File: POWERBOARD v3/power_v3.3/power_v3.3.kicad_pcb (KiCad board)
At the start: 4 copper layers, 60 x 34.1 mm, 63 parts, among them IC1 MAX25301AATB_V+T, IC2 MCP6541T-I_OT, IC3 AP2281-1FMG-7, J1 43650-0300, J2 UJ20-C-H-G-SMT-1-P16-TR, J3 2053380002, U1 USBLC6-2, U2 BQ25886RGE, U3 TPS62160DSG

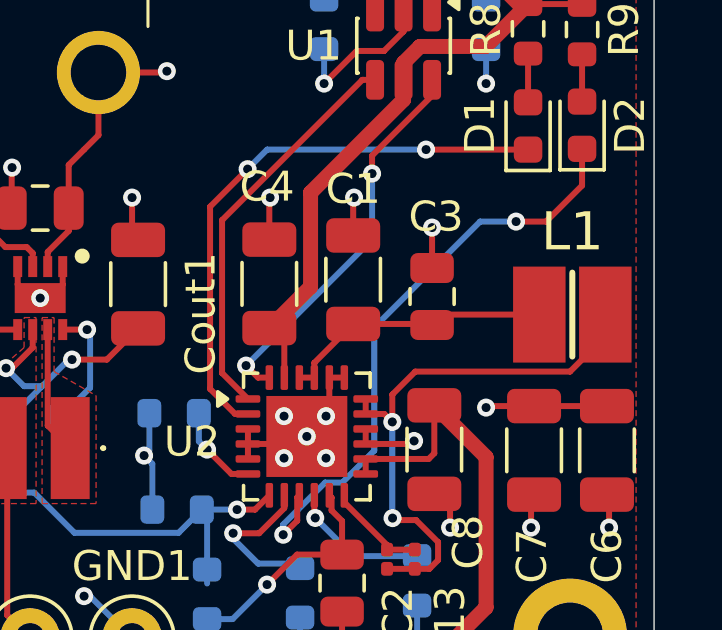
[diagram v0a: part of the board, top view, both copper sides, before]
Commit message: Widened PMID trace
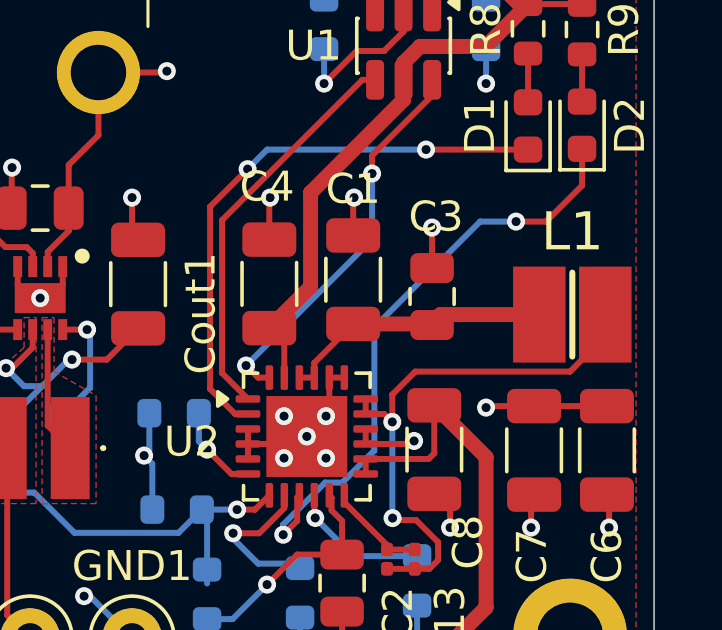
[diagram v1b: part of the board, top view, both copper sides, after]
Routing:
- net /Charging circuit/PMID: track 9.19 -> 9.90 mm
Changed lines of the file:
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@@
+	)
+	(segment
+		(start 184.2775 88.815)
+		(end 183.965 89.1275)
+		(width 0.5)
+		(layer "F.Cu")
+		(net "/Charging circuit/PMID")
 	)
 	(segment
 		(start 181.37 89.1275)
 		(end 183.965 89.1275)
-		(width 0.2)
+		(width 0.5)
 		(layer "F.Cu")
 		(net "/Charging circuit/PMID")
 	)
 	(segment
-		(start 184.5 88.815)
+		(start 184.2775 88.815)
 		(end 187.575 88.815)
-		(width 0.2)
+		(width 0.5)
 		(layer "F.Cu")
 		(net "/Charging circuit/PMID")
+	)
+	(segment
+		(start 187.54 88.78)
+		(end 187.575 88.815)
+		(width 1)
+		(layer "F.Cu")
+		(net "/Charging circuit/PMID")

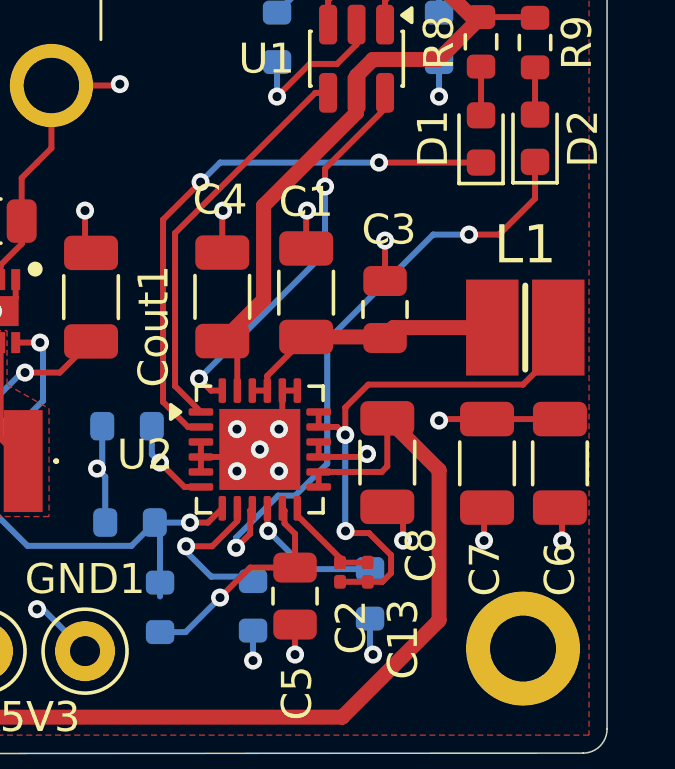
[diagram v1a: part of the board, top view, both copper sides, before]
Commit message: Widened SW trace
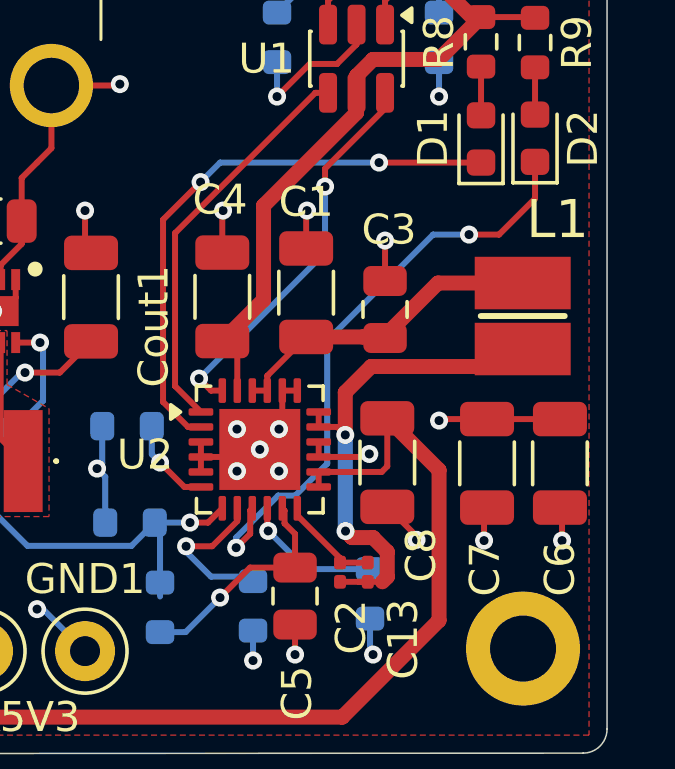
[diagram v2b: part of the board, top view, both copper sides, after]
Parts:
- moved L1 0.39 mm to (188.6, 88.4), turned to -90 degrees
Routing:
- net /Charging circuit/PMID: track 9.90 -> 11.5 mm
- net /Charging circuit/SW: track 18.5 -> 17.9 mm
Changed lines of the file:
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@@
 	(footprint "74438336010:INDC3030X200N"
 		(layer "F.Cu")
-		(at 188.675 88.815)
+		(at 188.59 88.43 -90)
 		(descr "74438336010*-*-")
 		(tags "Inductor")
 		(property "Reference" "L1"
-			(at 0 -2.7625 0)
+			(at -3.22 -1.16 0)
 			(layer "F.SilkS")
 			(effects
@@
 		)
 		(property "Value" "1u"
-			(at 0 0 0)
+			(at 0 0 90)
 			(layer "F.SilkS")
 			(hide yes)
@@
 		)
 		(property "Datasheet" "https://www.mouser.ch/datasheet/3/76/2/J_E_TE243A_0017.pdf"
-			(at 0 0 0)
+			(at 0 0 90)
 			(layer "F.Fab")
 			(hide yes)
@@
 		)
 		(property "Description" "DFE252012F"
-			(at 0 0 0)
+			(at 0 0 90)
 			(layer "F.Fab")
 			(hide yes)
@@
 		)
 		(fp_line
-			(start -2.225 -1.85)
-			(end 2.225 -1.85)
+			(start -2.225 1.85)
+			(end -2.225 -1.85)
 			(stroke
 				(width 0.05)
@@
 		)
 		(fp_line
-			(start -2.225 1.85)
-			(end -2.225 -1.85)
+			(start 2.225 1.85)
+			(end -2.225 1.85)
 			(stroke
 				(width 0.05)
@@
 		)
 		(fp_line
-			(start 2.225 -1.85)
-			(end 2.225 1.85)
+			(start -2.225 -1.85)
+			(end 2.225 -1.85)
 			(stroke
 				(width 0.05)
@@
 		)
 		(fp_line
-			(start 2.225 1.85)
-			(end -2.225 1.85)
+			(start 2.225 -1.85)
+			(end 2.225 1.85)
 			(stroke
 				(width 0.05)
@@
 		)
 		(fp_line
-			(start -1.5 -1.5)
-			(end 1.5 -1.5)
+			(start -1.5 1.5)
+			(end -1.5 -1.5)
 			(stroke
 				(width 0.1)
@@
 		)
 		(fp_line
-			(start -1.5 1.5)
-			(end -1.5 -1.5)
+			(start 1.5 1.5)
+			(end -1.5 1.5)
 			(stroke
 				(width 0.1)
@@
 		)
 		(fp_line
-			(start 1.5 -1.5)
-			(end 1.5 1.5)
+			(start -1.5 -1.5)
+			(end 1.5 -1.5)
 			(stroke
 				(width 0.1)
@@
 		)
 		(fp_line
-			(start 1.5 1.5)
-			(end -1.5 1.5)
+			(start 1.5 -1.5)
+			(end 1.5 1.5)
 			(stroke
 				(width 0.1)
@@
 		)
 		(fp_text user "${REFERENCE}"
-			(at 0 -2.7625 0)
+			(at 0 -2.7625 90)
 			(layer "F.Fab")
 			(effects
@@
 		)
 		(pad "1" smd rect
-			(at -1.1 0)
+			(at -1.1 0 270)
 			(size 1.75 3.2)
 			(layers "F.Cu" "F.Mask" "F.Paste")
@@
 		)
 		(pad "2" smd rect
-			(at 1.1 0)
+			(at 1.1 0 270)
 			(size 1.75 3.2)
 			(layers "F.Cu" "F.Mask" "F.Paste")
@@
 	)
 	(segment
-		(start 183.440256 90.715)
-		(end 188.6 90.715)
+		(start 183.13 97.29)
+		(end 183.425 97.29)
 		(width 0.2)
 		(layer "F.Cu")
@@
 	)
 	(segment
-		(start 183.91 97.29)
-		(end 184.2 97)
+		(start 182.5 97.29)
+		(end 183.13 97.29)
 		(width 0.2)
 		(layer "F.Cu")
@@
 	)
 	(segment
-		(start 182.5 97.29)
-		(end 183.425 97.29)
-		(width 0.2)
+		(start 184.075 97.125)
+		(end 184.075 96.29)
+		(width 0.5)
 		(layer "F.Cu")
 		(net "/Charging circuit/SW")
@@
 	)
 	(segment
-		(start 188.6 90.715)
-		(end 189.775 89.54)
-		(width 0.2)
+		(start 183.91 97.29)
+		(end 184.075 97.125)
+		(width 0.5)
 		(layer "F.Cu")
 		(net "/Charging circuit/SW")
 	)
 	(segment
-		(start 183.425 97.29)
-		(end 183.91 97.29)
-		(width 0.2)
+		(start 182.898529 95.815)
+		(end 182.682769 95.59924)
+		(width 0.5)
 		(layer "F.Cu")
 		(net "/Charging circuit/SW")
 	)
 	(segment
-		(start 182.673942 91.481314)
-		(end 183.440256 90.715)
-		(width 0.2)
+		(start 184.075 96.29)
+		(end 183.6 95.815)
+		(width 0.5)
 		(layer "F.Cu")
 		(net "/Charging circuit/SW")
 	)
 	(segment
-		(start 189.775 89.54)
-		(end 189.775 88.815)
-		(width 0.2)
+		(start 183.5375 90.1125)
+		(end 188.0075 90.1125)
+		(width 0.5)
 		(layer "F.Cu")
 		(net "/Charging circuit/SW")
 	)
 	(segment
-		(start 184.2 96.4)
-		(end 183.465 95.665)
+		(start 189.775 89.54)
+		(end 189.775 88.815)
 		(width 0.2)
 		(layer "F.Cu")
@@
 	)
 	(segment
-		(start 182.673942 92.392531)
-		(end 182.673942 91.481314)
-		(width 0.2)
+		(start 182.673942 90.976058)
+		(end 183.5375 90.1125)
+		(width 0.5)
 		(layer "F.Cu")
 		(net "/Charging circuit/SW")
@@
 	)
 	(segment
-		(start 183.465 95.665)
-		(end 182.748529 95.665)
-		(width 0.2)
+		(start 188.0075 90.1125)
+		(end 188.59 89.53)
+		(width 0.5)
+		(layer "F.Cu")
+		(net "/Charging circuit/SW")
+	)
+	(segment
+		(start 183.6 95.815)
+		(end 182.898529 95.815)
+		(width 0.5)
 		(layer "F.Cu")
 		(net "/Charging circuit/SW")
@@
 	)
 	(segment
-		(start 184.2 97)
-		(end 184.2 96.4)
+		(start 182.673942 92.392531)
+		(end 182.673942 90.976058)
+		(width 0.5)
+		(layer "F.Cu")
+		(net "/Charging circuit/SW")
+	)
+	(segment
+		(start 183.13 97.29)
+		(end 183.91 97.29)
 		(width 0.2)
 		(layer "F.Cu")
@@
 		(start 182.673942 95.590413)
 		(end 182.673942 92.392531)
-		(width 0.2)
+		(width 0.5)
 		(layer "B.Cu")
 		(net "/Charging circuit/SW")
@@
 	)
 	(segment
-		(start 184.2775 88.815)
-		(end 183.965 89.1275)
-		(width 0.5)
-		(layer "F.Cu")
-		(net "/Charging circuit/PMID")
-	)
-	(segment
 		(start 181.37 89.1275)
-		(end 183.965 89.1275)
+		(end 183.25 89.1275)
 		(width 0.5)
 		(layer "F.Cu")
@@
 	)
 	(segment
-		(start 184.2775 88.815)
-		(end 187.575 88.815)
+		(start 185.7625 87.33)
+		(end 188.59 87.33)
 		(width 0.5)
 		(layer "F.Cu")
@@
 	)
 	(segment
-		(start 187.54 88.78)
-		(end 187.575 88.815)
-		(width 1)
+		(start 183.965 89.1275)
+		(end 185.7625 87.33)
+		(width 0.5)
 		(layer "F.Cu")
 		(net "/Charging circuit/PMID")
@@
 	)
 	(segment
+		(start 183.25 89.1275)
+		(end 183.965 89.1275)
+		(width 0.5)
+		(layer "F.Cu")
+		(net "/Charging circuit/PMID")
+	)
+	(segment
 		(start 183.965 89.1275)
 		(end 184 89.1625)
@@
 	)
 	(segment
+		(start 185.05 95.765)
+		(end 184.075 94.79)
+		(width 0.2)
+		(layer "F.Cu")
+		(net "GND")
+	)
+	(segment
 		(start 169.9875 83.9275)
 		(end 170 83.915)
@@
 	)
 	(segment
-		(start 184.6 95.315)
-		(end 184.075 94.79)
-		(width 0.2)
-		(layer "F.Cu")
-		(net "GND")
-	)
-	(segment
 		(start 171.6875 87.815)
 		(end 171.2375 88.265)
@@
 	)
 	(segment
-		(start 184.6 95.915)
-		(end 184.6 95.315)
-		(width 0.2)
-		(layer "F.Cu")
-		(net "GND")
-	)
-	(segment
 		(start 180.575 90.915)
 		(end 180.575 92.09)
@@
 	)
 	(segment
+		(start 185.05 95.89)
+		(end 185.05 95.765)
+		(width 0.2)
+		(layer "F.Cu")
+		(net "GND")
+	)
+	(segment
 		(start 178.8 73.515)
 		(end 178.8 73.115)
@@
 	)
 	(via
-		(at 184.6 95.915)
+		(at 185.05 95.89)
 		(size 0.6)
 		(drill 0.3)
@@
 	)
 	(segment
+		(start 183.475 93.0275)
+		(end 183.4 93.0275)
+		(width 0.2)
+		(layer "F.Cu")
+		(net "/Charging circuit/SYS")
+	)
+	(segment
 		(start 171.1875 87.215)
 		(end 171.1875 87.3025)
@@
 	)
 	(segment
-		(start 181.7875 93.1275)
-		(end 181.7875 92.6275)
+		(start 183.4 93.0275)
+		(end 183.3 93.1275)
 		(width 0.2)
 		(layer "F.Cu")
@@
 	)
 	(segment
-		(start 171.1875 86.7275)
-		(end 171.8875 86.0275)
+		(start 181.7875 93.1275)
+		(end 181.7875 92.6275)
 		(width 0.2)
 		(layer "F.Cu")
@@
 	)
 	(segment
-		(start 183.3 93.1275)
-		(end 183.4 93.0275)
+		(start 171.1875 86.7275)
+		(end 171.8875 86.0275)
 		(width 0.2)
 		(layer "F.Cu")
@@
 	)
 	(segment
+		(start 183.3 93.1275)
+		(end 181.7875 93.1275)
+		(width 0.2)
+		(layer "F.Cu")
+		(net "/Charging circuit/SYS")
+	)
+	(segment
 		(start 172.8795 80.746)
 		(end 172.8795 82.8355)
@@
 	)
 	(segment
-		(start 181.7875 93.1275)
-		(end 183.3 93.1275)
-		(width 0.2)
-		(layer "F.Cu")
-		(net "/Charging circuit/SYS")
-	)
-	(segment
 		(start 171.2 87.315)
 		(end 171.1875 87.3025)
@@
 	)
 	(via
-		(at 183.4 93.0275)
+		(at 183.475 93.0275)
 		(size 0.6)
 		(drill 0.3)
